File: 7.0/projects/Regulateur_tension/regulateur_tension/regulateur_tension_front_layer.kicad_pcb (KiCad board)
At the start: 2 copper layers, 81.3 x 50.8 mm, 11 parts

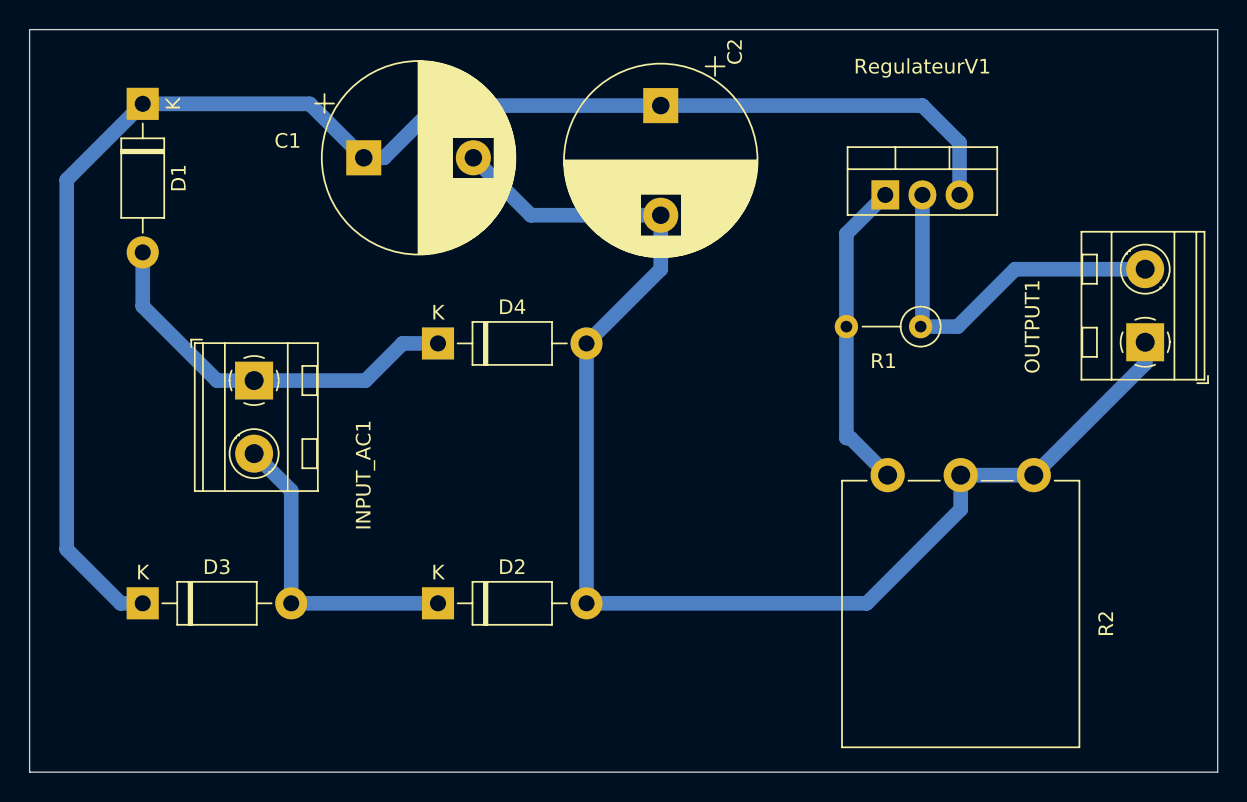
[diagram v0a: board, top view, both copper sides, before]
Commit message: addition exercie control daccess -cirucit transfo
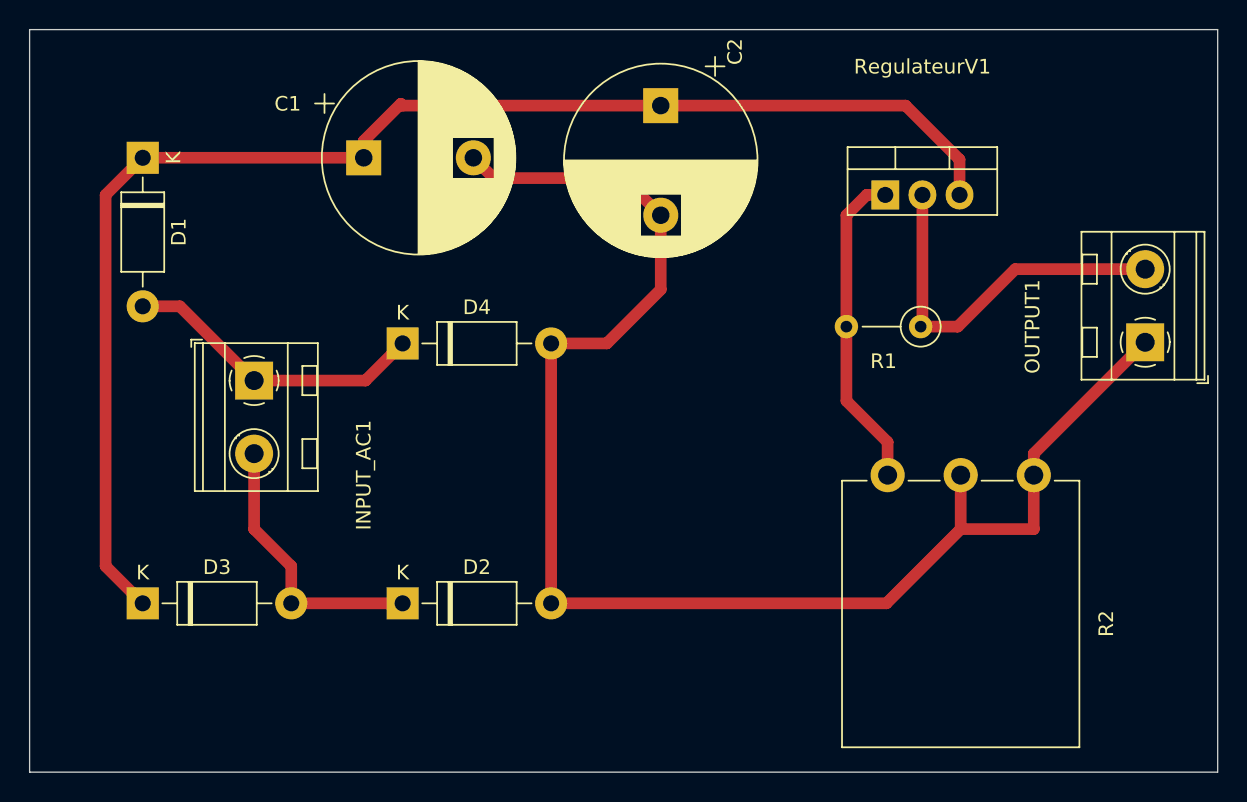
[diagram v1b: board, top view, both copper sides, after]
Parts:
- moved D1 3.69 mm to (23.0, 24.0)
- moved D2 2.42 mm to (40.8, 54.5)
- moved D4 2.42 mm to (40.8, 36.7)
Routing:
- net GND: track 91.0 -> 101.1 mm
- net Net-(D1-K): track 103.0 -> 94.7 mm
- net Net-(D1-A): track 27.0 -> 20.9 mm
- net Net-(D2-K): track 21.3 -> 18.9 mm
- net Net-(RegulateurV1-ADJ): track 21.6 -> 22.2 mm
